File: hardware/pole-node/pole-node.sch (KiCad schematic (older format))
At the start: 31 parts, among them J1 Anderson, J2 RJ45, J3 Conn_01x02, J4 Conn_01x03, J5 Conn_01x03, J6 Conn_01x03, U1 AP3211, U2 MAX485E, U3 MAX485E

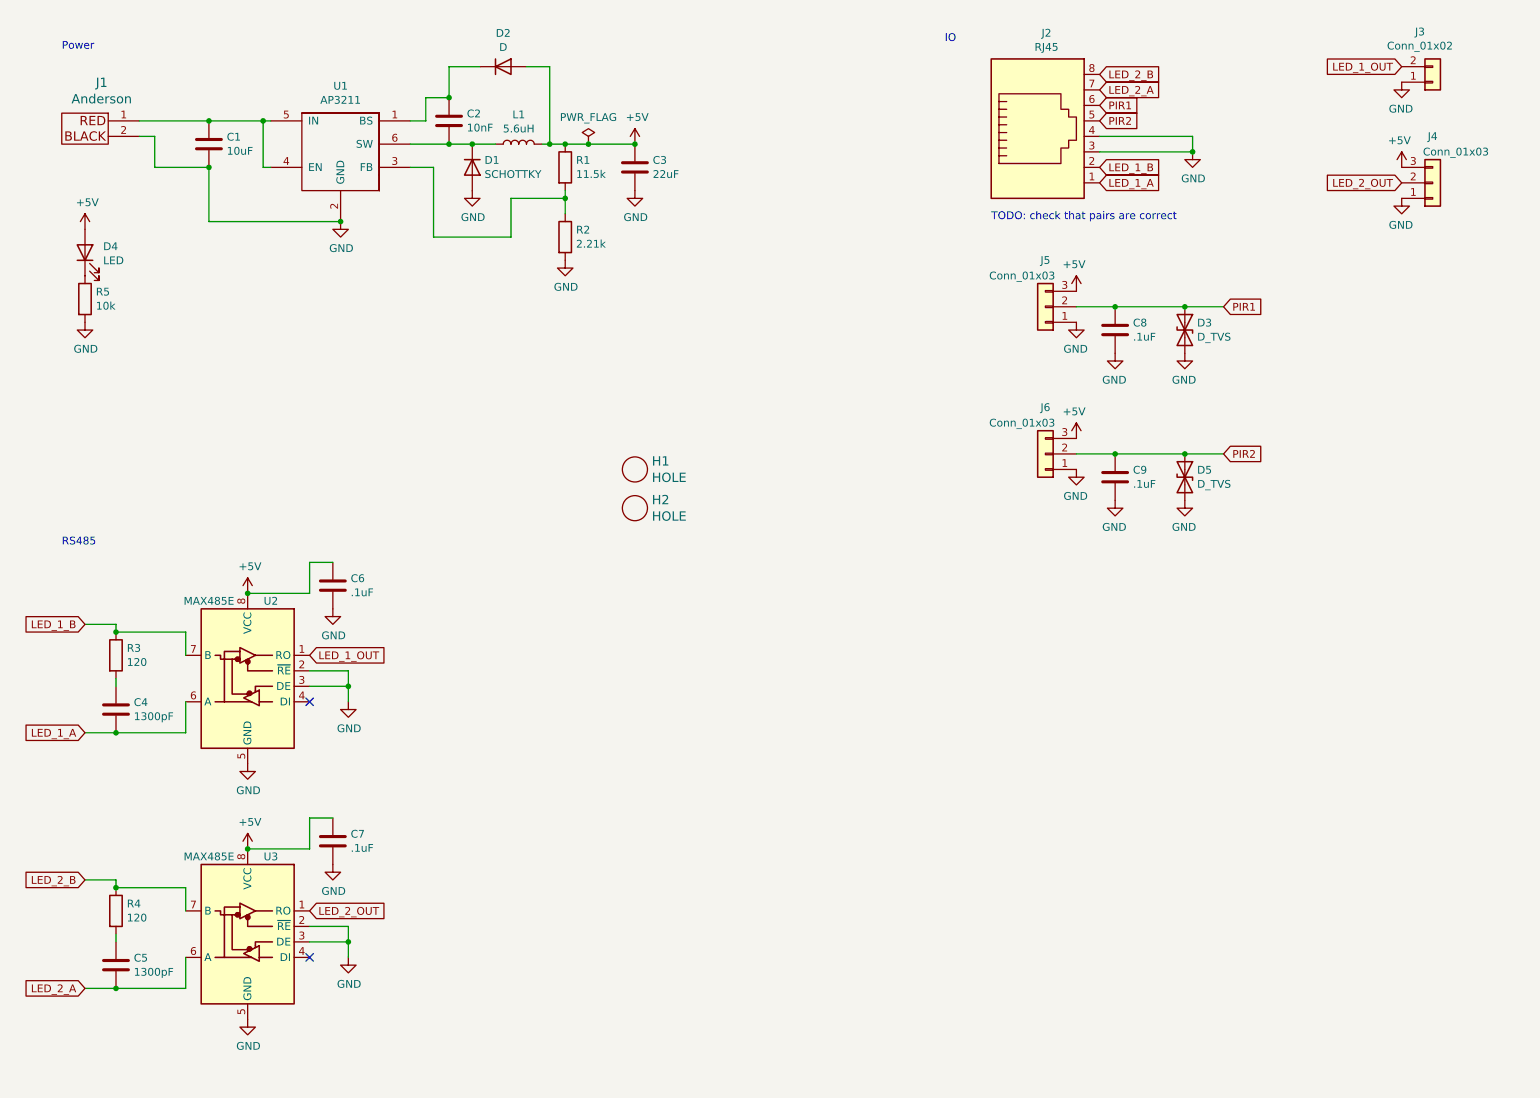
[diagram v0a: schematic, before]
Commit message: Update pole node to v1.1
This adds lots of TVS diode, more decoupling, bulk caps on 5v and 12v
lines. Also adds pass-through Anderson connector.
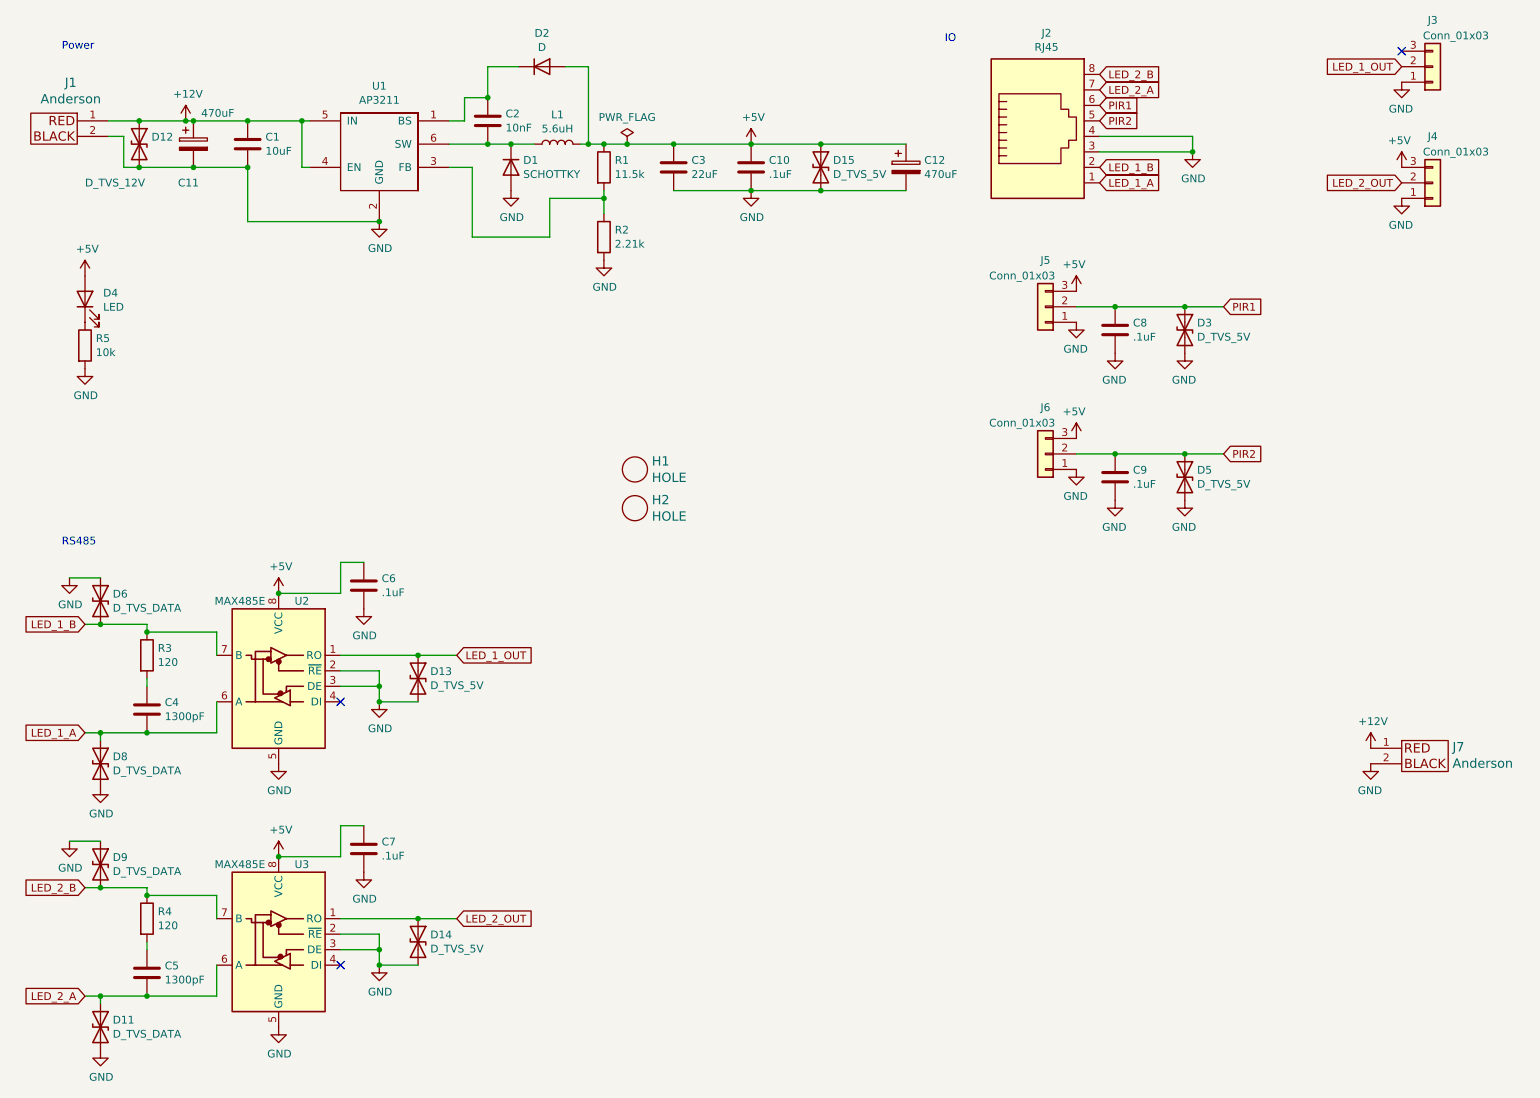
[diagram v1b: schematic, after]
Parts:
- removed J3: Conn_01x02, Connector_PinHeader_2.54mm:PinHeader_1x02_P2.54mm_Vertical, symbol Connector_Generic:Conn_01x02
- added C10: .1uF, Capacitor_SMD:C_0603_1608Metric, symbol Device:C
- added C11, C12: 470uF, Capacitor_THT:CP_Radial_D10.0mm_P5.00mm, symbol Device:CP
- added D11, D6, D8, D9: D_TVS_DATA, Diode_SMD:D_SMB, symbol Device:D_TVS
- added D12: D_TVS_12V, Diode_SMD:D_SMB, symbol Device:D_TVS
- added D13, D14, D15: D_TVS_5V, Diode_SMD:D_SMB, symbol Device:D_TVS
- added J3: Conn_01x03, Connector_PinHeader_2.54mm:PinHeader_1x03_P2.54mm_Horizontal, symbol Connector_Generic:Conn_01x03
- added J7: Anderson, homebrew:Anderson_1336G1_right_angle_bottom_two, symbol Homebrew:Anderson_two_redblack_sink
- C2, C4, C5: MPN (none) -> CL10B122KB8NNNC
- C3: MPN (none) -> LMK212BBJ226MG-T
- D1: MPN (none) -> MBR230LSTR
- D2: MPN (none) -> 1N4148WS-7-F
- D3, D5: value D_TVS -> D_TVS_5V; footprint Diode_SMD:D_SOD-523 -> Diode_SMD:D_SMB; MPN (none) -> SMBJ6.0CD-M3/H
- D4: MPN (none) -> 150060RS75000
- J1: footprint homebrew:Anderson_1337G3_right_angle_bottom_two -> homebrew:Anderson_1336G1_right_angle_bottom_two
- J2: MPN (none) -> 54601-908WPLF
- J4, J5, J6: footprint Connector_PinHeader_2.54mm:PinHeader_1x03_P2.54mm_Vertical -> Connector_PinHeader_2.54mm:PinHeader_1x03_P2.54mm_Horizontal; MPN (none) -> 78208-103HLF
- L1: MPN (none) -> NR6028T6R0M
- R1: MPN (none) -> RMCF0603FT11K5
- R2: MPN (none) -> RC1608F2211CS
- R3, R4: MPN (none) -> RMCF0603JG120R
- U1: MPN (none) -> AP3211KTR-G1
- U2, U3: MPN (none) -> SP485ECN-L/TR
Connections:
- net +5V: now also C10.1, C12.1, D15.1 (A1)
- net GND: now also C10.2, C11.2, C12.2, D11.2 (A2), D12.2 (A2), D13.2 (A2), D14.2 (A2), D15.2 (A2), D6.1 (A1), D8.2 (A2), D9.1 (A1), J3.1 (Pin_1), J7.2
- net LED_1_A: now also D8.1 (A1)
- net LED_1_B: now also D6.2 (A2)
- net LED_1_OUT: now also D13.1 (A1), J3.2 (Pin_2)
- net LED_2_A: now also D11.1 (A1)
- net LED_2_B: now also D9.2 (A2)
- net LED_2_OUT: now also D14.1 (A1)
- net +12V: now reaches C1.1, J1.1, U1.4 (EN), U1.5 (IN)
- net +12V: now also C11.1, D12.1 (A1), J7.1
- no-connect marks 2 -> 3
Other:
- note removed: "TODO: check that pairs are correct"
- moved on the sheet: C1, C2, C3, C4, C5, C6, C7, D1, D2, D4, J1, L1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

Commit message: Random hardware changes
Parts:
- H1, H2: symbol Homebrew:HOLE -> pole-node-rescue:HOLE-Homebrew
- J1: symbol Homebrew:Anderson_two_redblack_src -> pole-node-rescue:Anderson_two_redblack_src-Homebrew
- J7: symbol Homebrew:Anderson_two_redblack_sink -> pole-node-rescue:Anderson_two_redblack_sink-Homebrew
- U1: symbol Homebrew:AP3211 -> pole-node-rescue:AP3211-Homebrew
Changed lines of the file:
@@
 $EndDescr
 $Comp
-L Homebrew:AP3211 U1
+L pole-node-rescue:AP3211-Homebrew U1
 U 1 1 5E594E3E
 P 2800 1400
@@
 	4400 1400 4700 1400
 $Comp
-L Homebrew:Anderson_two_redblack_src J1
+L pole-node-rescue:Anderson_two_redblack_src-Homebrew J1
 U 1 1 5E5A16EF
 P 700 1300
@@
 $EndComp
 $Comp
-L Homebrew:HOLE H1
+L pole-node-rescue:HOLE-Homebrew H1
 U 1 1 5E650CB4
 P 4450 3500
@@
 $EndComp
 $Comp
-L Homebrew:HOLE H2
+L pole-node-rescue:HOLE-Homebrew H2
 U 1 1 5E652DE7
 P 4450 3750
@@
 $EndComp
 $Comp
-L Homebrew:Anderson_two_redblack_sink J7
+L pole-node-rescue:Anderson_two_redblack_sink-Homebrew J7
 U 1 1 607786F1
 P 9550 5350
